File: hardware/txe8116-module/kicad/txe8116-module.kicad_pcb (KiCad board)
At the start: 2 copper layers, 59.8 x 42.4 mm, 1 part

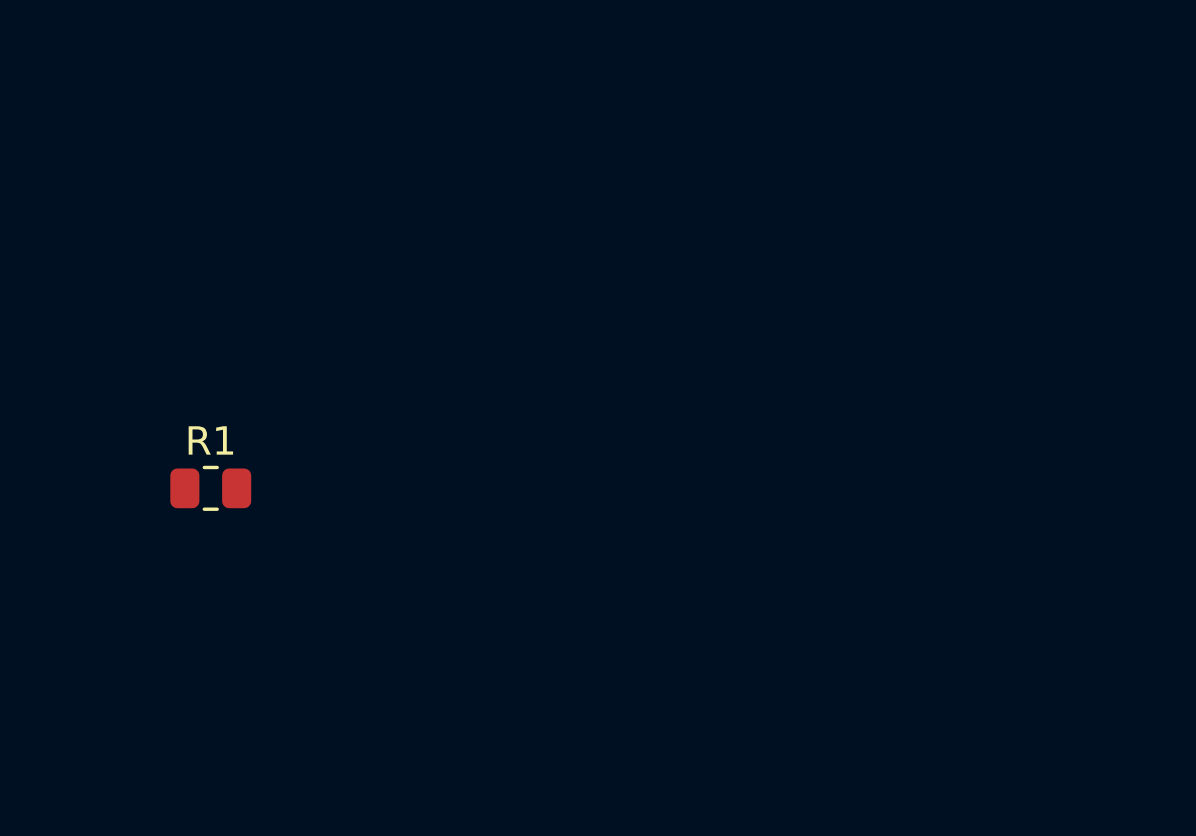
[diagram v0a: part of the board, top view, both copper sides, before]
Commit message: Add screw terminal footprint and update schematic
- Introduced a new screw terminal footprint (WAGO 2601-1102) in the PCB layout.
- Updated net connections for the new terminal block.
- Modified the resistor value in the schematic to 100k.
- Added a new connector symbol for the screw terminal in the schematic.
- Enhanced the schematic with additional wire connections for better clarity.
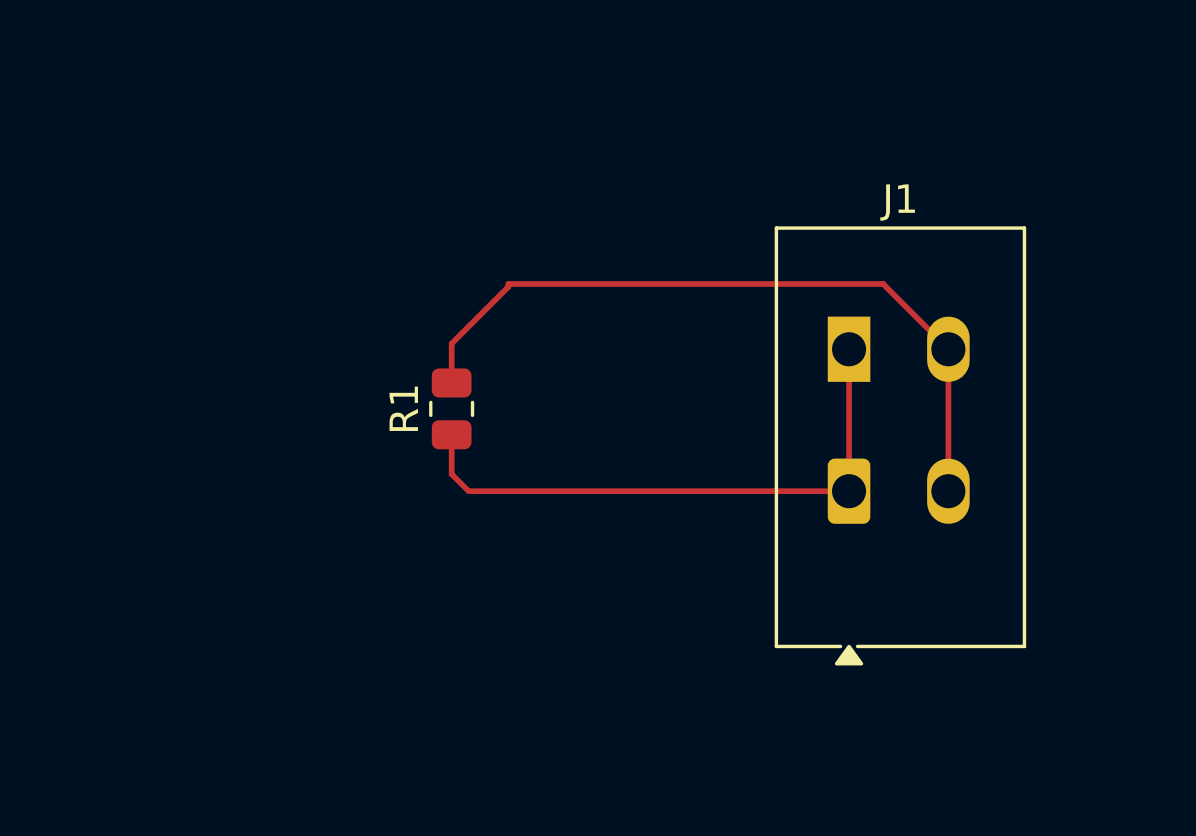
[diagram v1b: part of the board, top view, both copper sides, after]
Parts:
- added J1: Screw_Terminal_01x02, TerminalBlock_WAGO:TerminalBlock_WAGO_2601-1102_1x02_P3.50mm_Horizontal, F.Cu at (170.5, 86.4)
- R1: value R_Small -> 100k
- moved R1 8.94 mm to (156.5, 83.5), turned to 90 degrees
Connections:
- R1 pad 1: unconnected-(R1-Pad1) -> Net-(J1-Pin_1)
- R1 pad 2: unconnected-(R1-Pad2) -> Net-(J1-Pin_2)
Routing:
- net Net-(J1-Pin_2): track 0.00 -> 25.8 mm
- net Net-(J1-Pin_1): track 0.00 -> 20.6 mm

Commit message: Added some components
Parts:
- added U1: TXE8116, txe8116:Texas_DGS0024A_TSSOP-24_3x6.1mm_P0.5mm, F.Cu at (143.8, 78.5)
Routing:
- added copper zone on F.Cu, net (none)
